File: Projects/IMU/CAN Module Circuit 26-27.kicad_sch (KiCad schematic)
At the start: 10 parts, among them U1 TJA1050DRG, U2 MCP2515-I, X1 ${ALTIUM_VALUE}

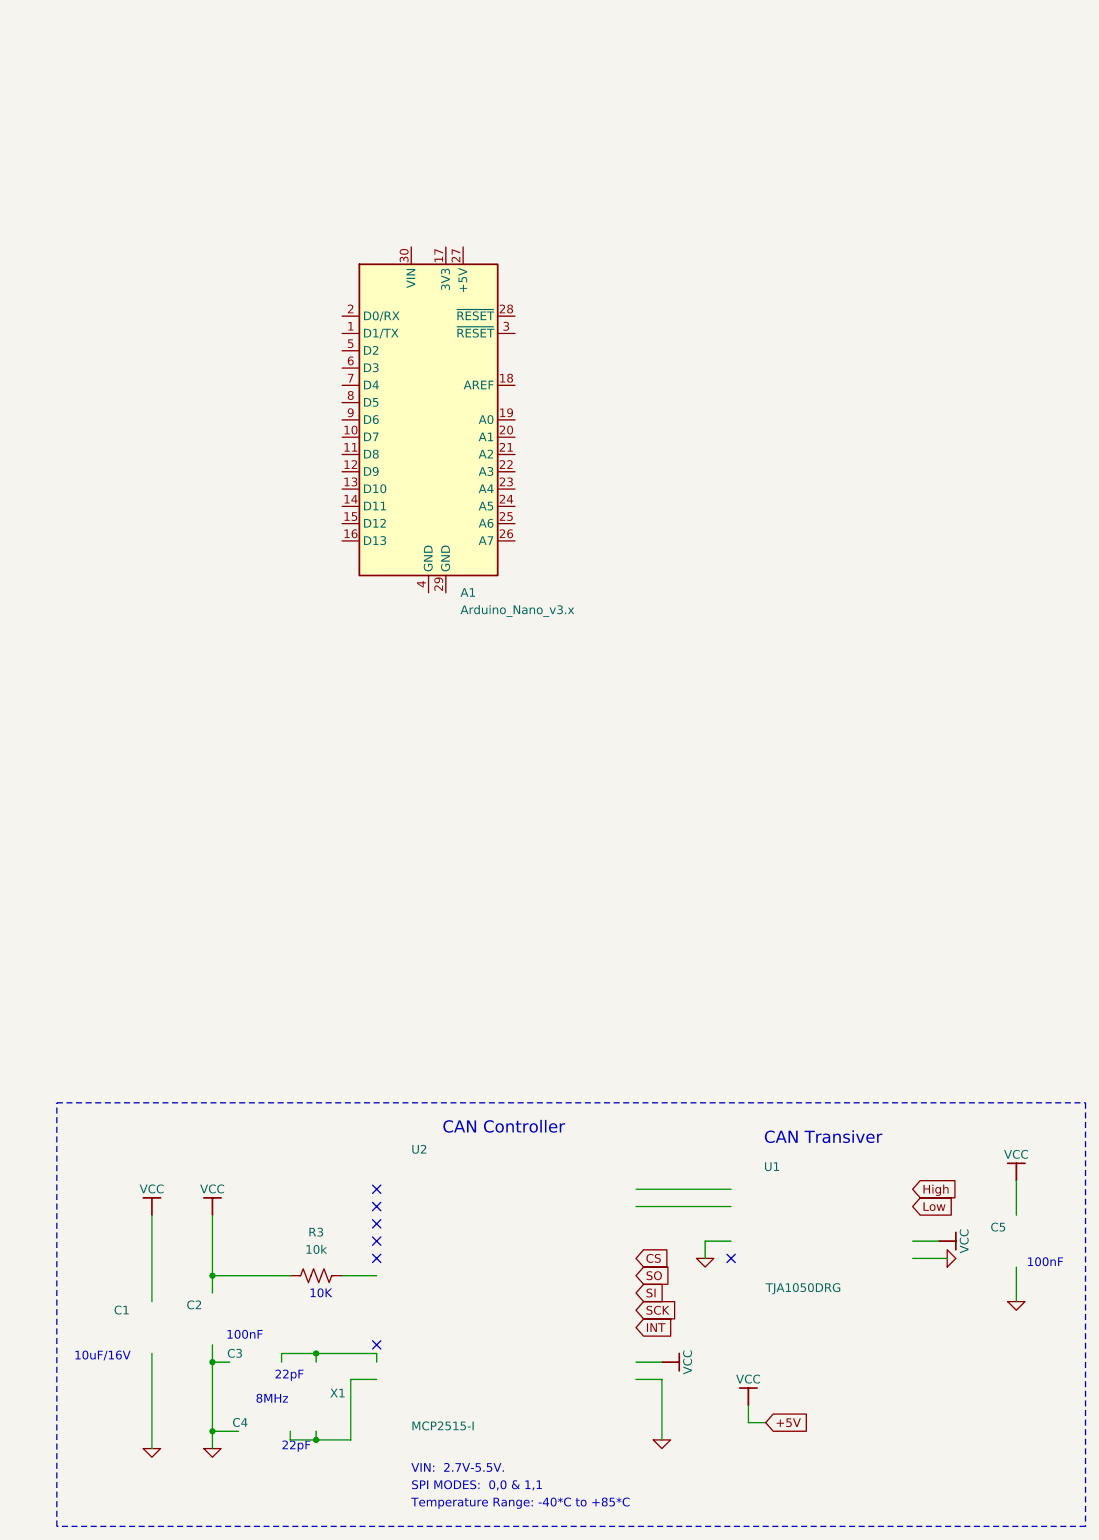
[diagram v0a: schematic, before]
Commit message: TM171
Completed TM171 footprint and UART connections.
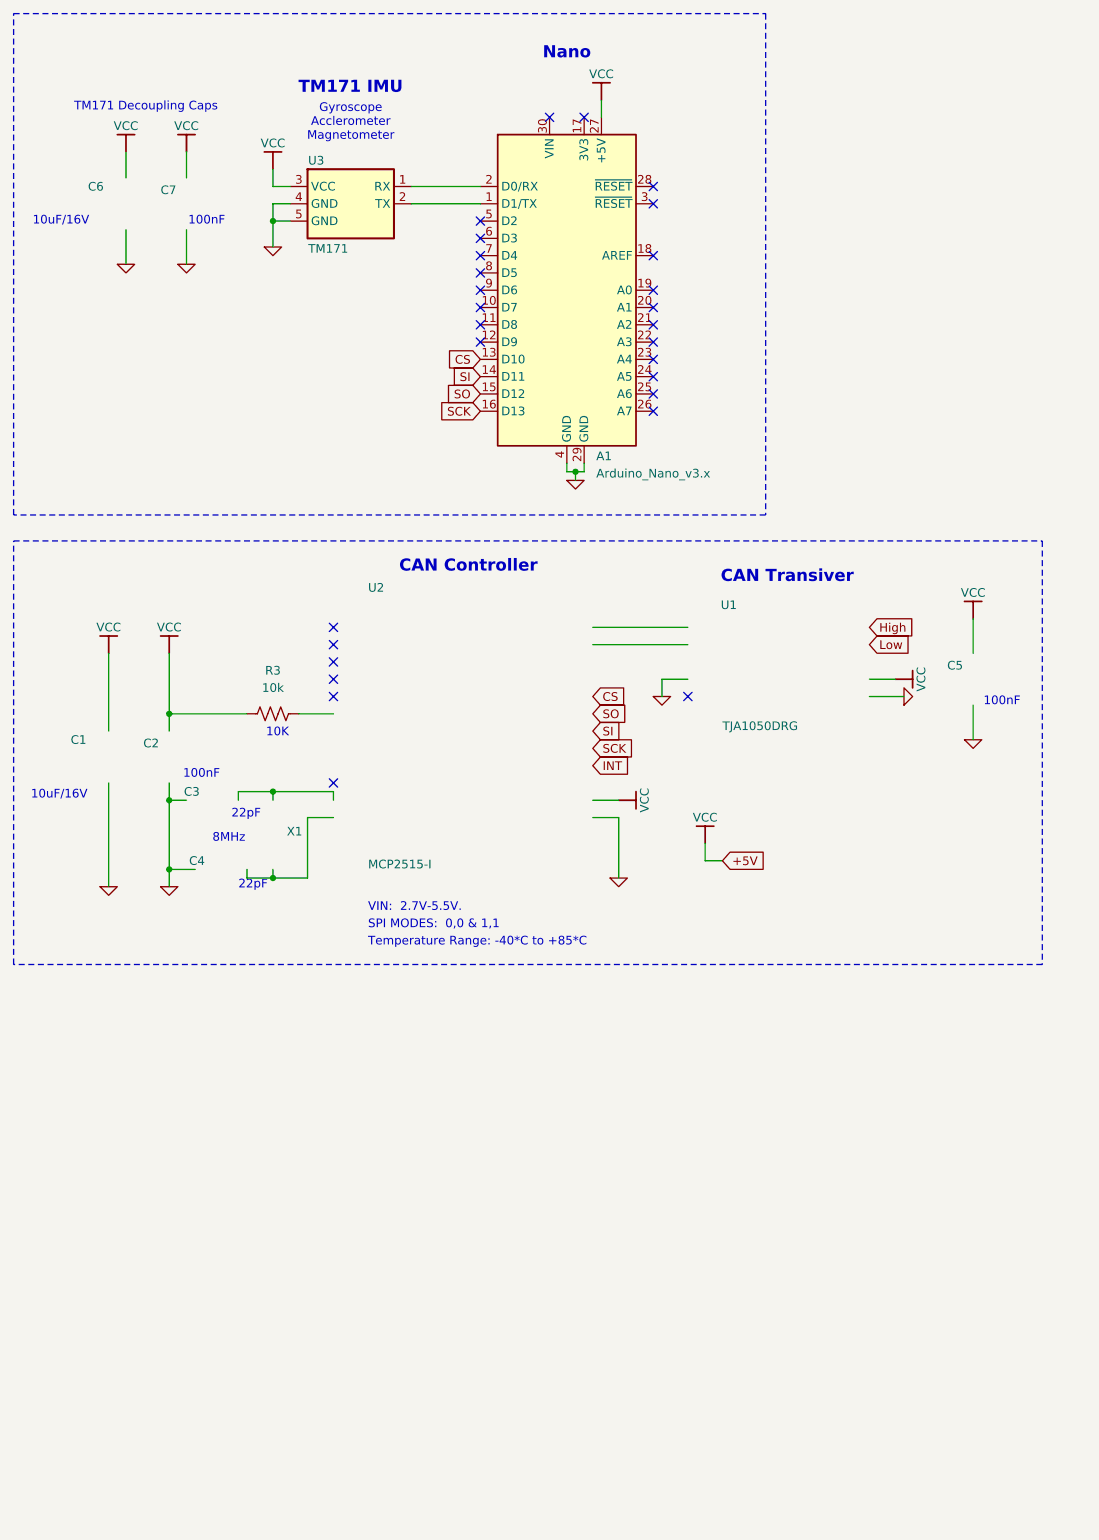
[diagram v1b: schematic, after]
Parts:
- added C6: 10uF/16V, Capacitor_THT:CP_Radial_Tantal_D5.0mm_P2.50mm, symbol CAN Integration-altium-import:root_0_Cap_Tantalum_adafruit.IntLib
- added C7: ${ALTIUM_VALUE}, Capacitor_THT:CP_Radial_D5.0mm_P2.50mm, symbol CAN Integration-altium-import:root_2_Cap_0603_adafruit.IntLib
- added U3: TM171, TransducerM:Transducer TM171, symbol TransducerM_TM171:TM171
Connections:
- net 0: now also A1.29 (GND), A1.4 (GND), U3.4 (GND), U3.5 (GND)
- net CS: now also A1.13 (D10)
- net SCK: now also A1.16 (D13)
- net SI: now also A1.14 (D11)
- net SO: now also A1.15 (D12)
- net VCC: now also A1.27 (+5V), U3.3 (VCC)
- net at A1.1 (D1/TX): now also U3.2 (TX)
- net at A1.2 (D0/RX): now also U3.1 (RX)
- no-connect marks 7 -> 28
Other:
- note added: "Gyroscope Acclerometer Magnetometer"
- note added: "Nano"
- note added: "TM171 Decoupling Caps"
- note added: "TM171 IMU"
- moved on the sheet: A1, R3
